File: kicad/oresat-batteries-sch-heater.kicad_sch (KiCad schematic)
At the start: 20 parts, among them Q20 PMV45EN, Q21 PMV45EN, Q38 PMV45EN, Q39 PMV45EN, Q42 MOSFET-PCH-SOT23-6, Q43 MOSFET-PCH-SOT23-6

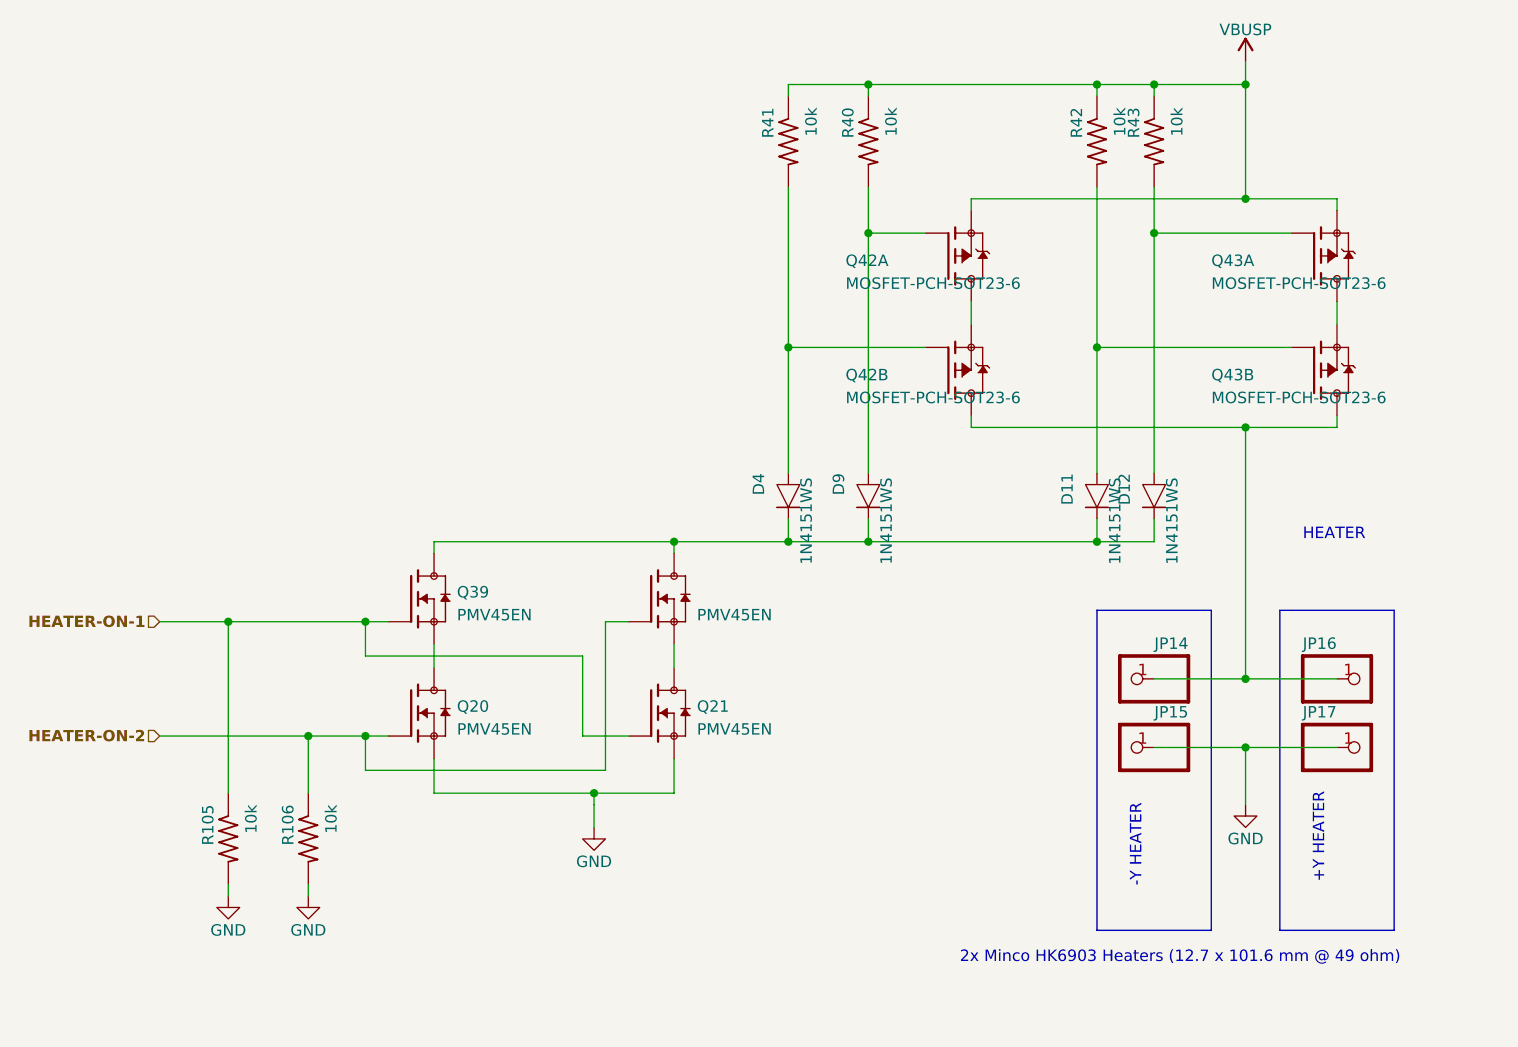
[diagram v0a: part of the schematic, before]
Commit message: Renovated Schematic
Updated schematic symbols and made more uniform with changed resistor, capacitor, and FET symbols. Changed 0603 cap foot print to 0603 small in Oresat passives. Added 2 new resistors and 2 new caps in the power page. Removed old debug connector in favor of the new one. The changes made should make very little updates when pushing the changes to the PCB.
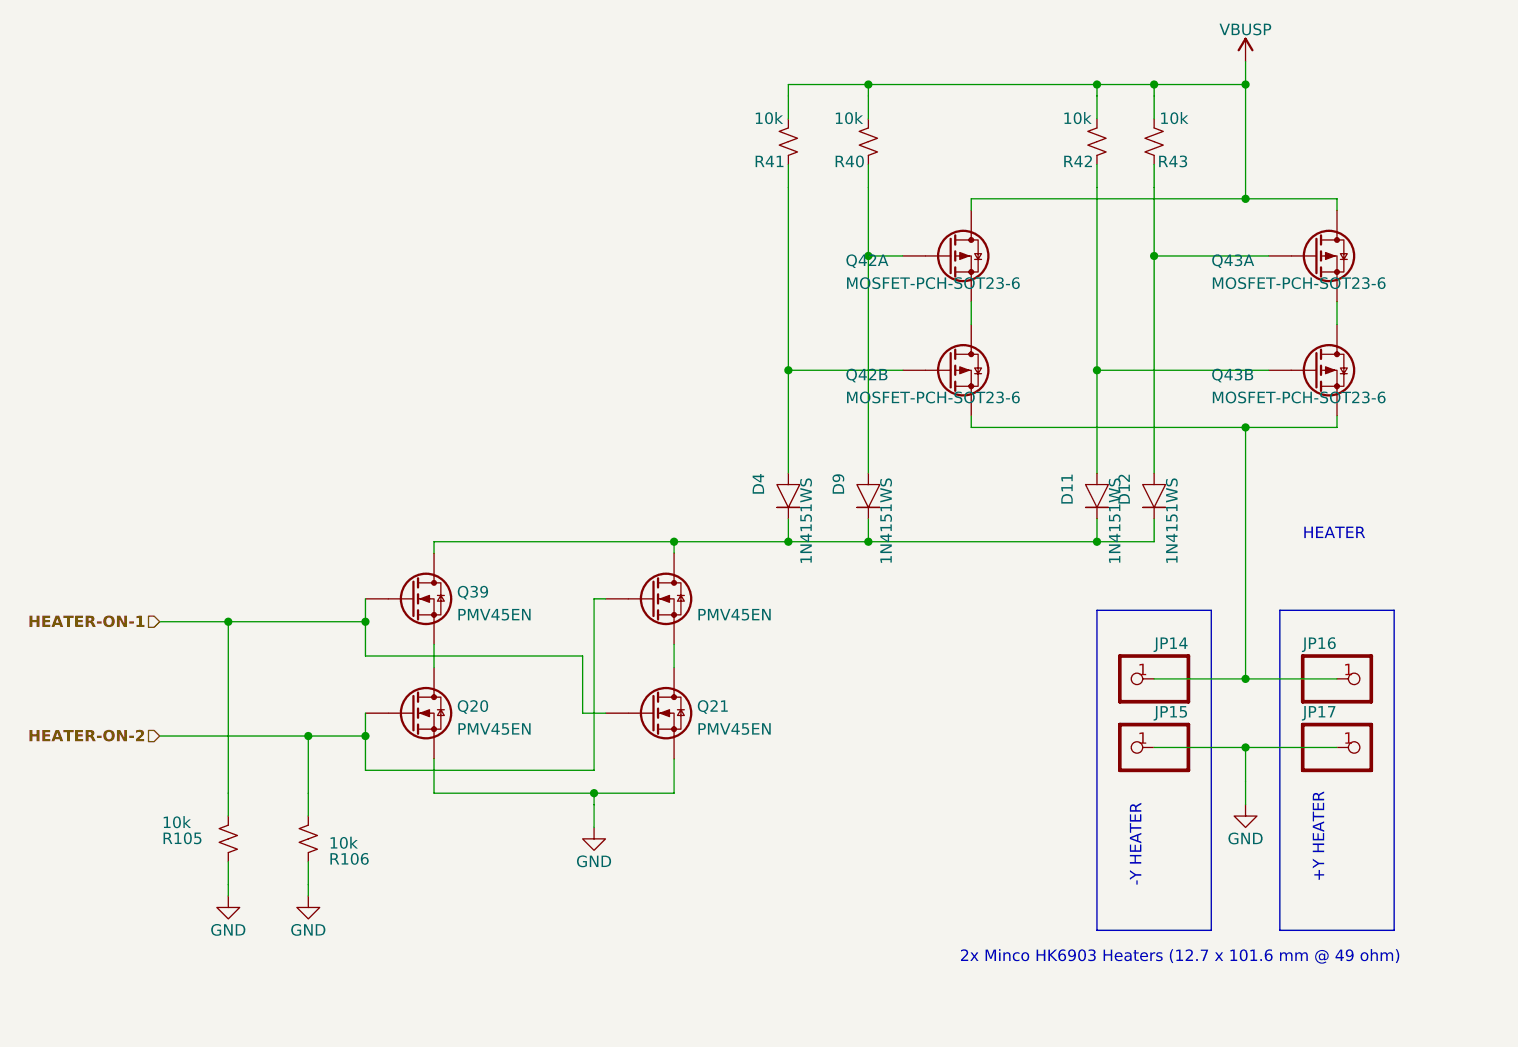
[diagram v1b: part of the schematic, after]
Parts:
- Q20, Q21, Q38, Q39: symbol oresat-batteries-eagle-import:N-MOSFET-SOT-23-3 -> Transistor_FET:Q_NMOS_GSD
- Q42, Q43: symbol oresat-batteries-eagle-import:Q-MOSFET-PCH-dual-SOT23-6_MOSFET-PCH-SOT23-6 -> Transistor_FET:Q_Dual_PMOS_G1S2G2D2S1D1
- R105, R106, R40, R41, R42, R43: symbol oresat-batteries-eagle-import:R-US_0603-C-NOSILK -> Device:R_Small_US
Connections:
- net GND: now also R105.1, R106.1; no longer R105.2, R106.2
- net HEATER-ON-1: now also R105.2; no longer R105.1
- net HEATER-ON-2: now also R106.2; no longer R106.1
- net VBUSP: now also Q42.6 (D), Q43.6 (D), R40.2, R41.2, R42.2, R43.2; no longer Q42.5 (S), Q43.5 (S), R40.1, R41.1, R42.1, R43.1
- net at D12.2, Q43.1 (G): now also R43.1; no longer R43.2
- net at Q42.2 (S): now also JP14.1, JP16.1, Q43.2 (S); no longer Q42.6 (D)
- net at D4.2, Q42.3 (G): now also R41.1; no longer R41.2
- net at D9.2, Q42.1 (G): now also R40.1; no longer R40.2
- net at D11.2, Q43.3 (G): now also R42.1; no longer R42.2
- new net: Q42.4 (D), Q42.5 (S)
- new net: Q43.4 (D), Q43.5 (S)

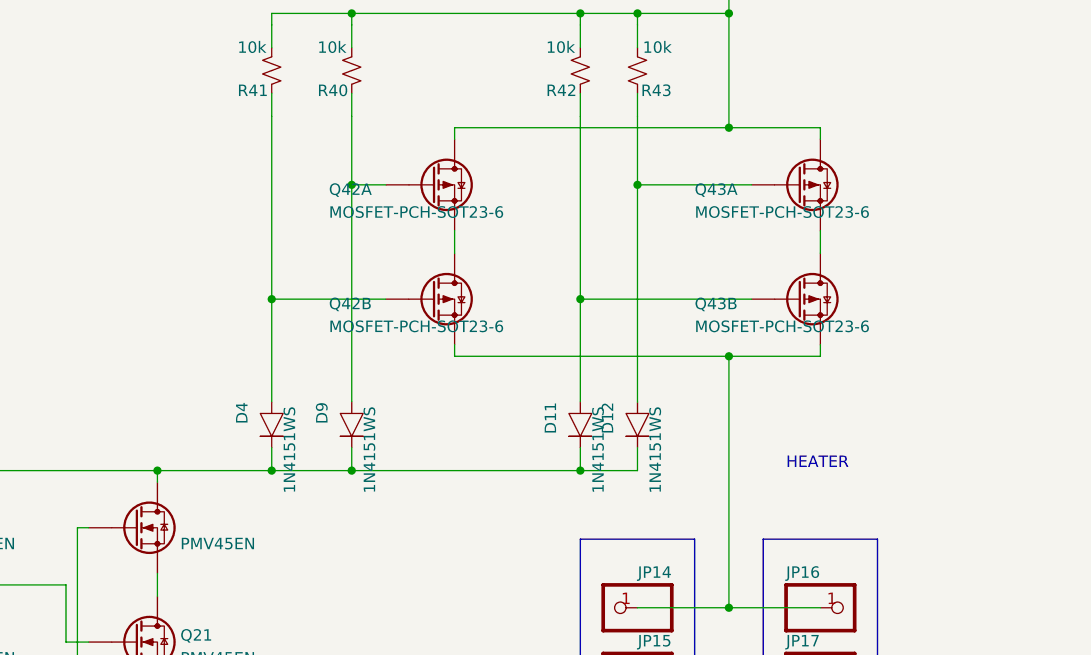
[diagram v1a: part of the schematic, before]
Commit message: Progress on v4
Figure out to bypass negative battery cutoff with 10k to make sure that nSHUTDOWN always works. Lots of moving around (it's tight), finally got pack 1 done. Working on the Pack 2.
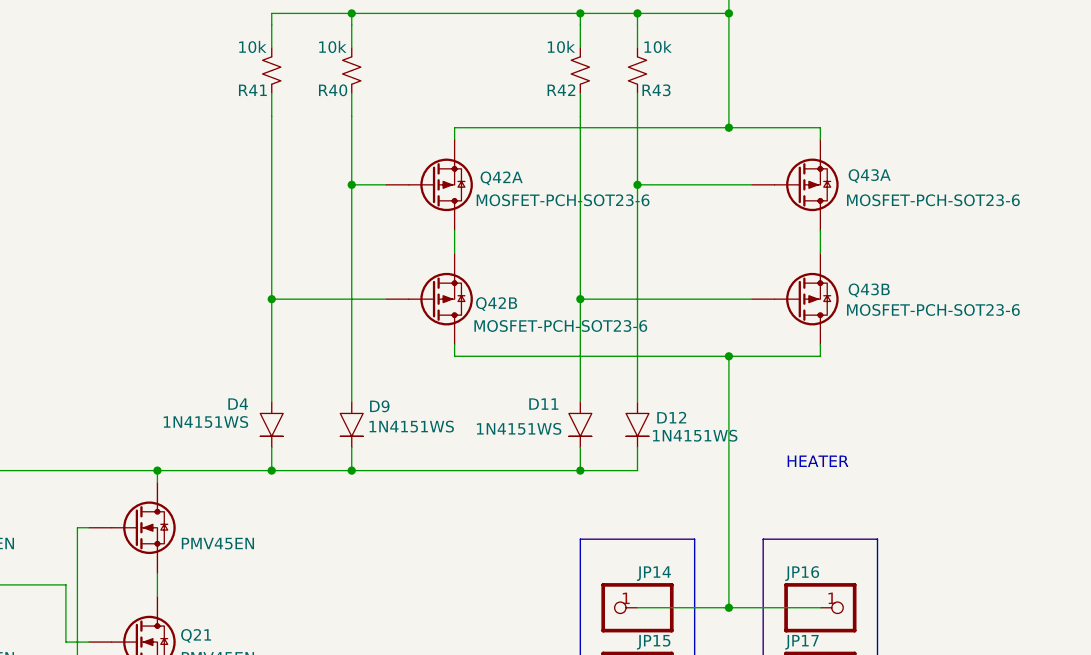
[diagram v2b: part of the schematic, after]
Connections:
- net VBUSP: now also Q42.5 (S), Q43.5 (S); no longer Q42.6 (D), Q43.6 (D)
- net at JP14.1, JP16.1: now also Q42.4 (D), Q43.4 (D); no longer Q42.2 (S), Q43.2 (S)
- new net: Q42.2 (S), Q42.6 (D)
- new net: Q43.2 (S), Q43.6 (D)
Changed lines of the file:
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@@
 		(dnp no)
 		(property "Reference" "D12"
-			(at 252.73 118.11 0)
+			(at 260.858 120.65 90)
 			(effects
 				(font
@@
 		)
 		(property "Value" "1N4151WS"
-			(at 256.54 128.27 0)
+			(at 256.794 121.158 90)
 			(effects
 				(font
@@
 		(lib_id "Transistor_FET:Q_Dual_PMOS_G1S2G2D2S1D1")
 		(at 232.41 106.68 0)
+		(mirror x)
 		(unit 2)
 		(exclude_from_sim no)
@@
 		(dnp no)
 		(property "Reference" "Q42"
-			(at 220.98 107.95 0)
+			(at 237.236 106.426 0)
 			(effects
 				(font
@@
 		)
 		(property "Value" "MOSFET-PCH-SOT23-6"
-			(at 220.98 110.49 0)
+			(at 236.982 108.966 0)
 			(effects
 				(font
@@
 		(dnp no)
 		(property "Reference" "D9"
-			(at 220.98 118.11 0)
+			(at 227.838 119.38 90)
 			(effects
 				(font
@@
 		)
 		(property "Value" "1N4151WS"
-			(at 224.79 128.27 0)
+			(at 225.298 120.142 90)
 			(effects
 				(font
@@
 		(lib_id "Transistor_FET:Q_Dual_PMOS_G1S2G2D2S1D1")
 		(at 273.05 106.68 0)
+		(mirror x)
 		(unit 2)
 		(exclude_from_sim no)
@@
 		(dnp no)
 		(property "Reference" "Q43"
-			(at 261.62 107.95 0)
+			(at 278.638 104.902 0)
 			(effects
 				(font
@@
 		)
 		(property "Value" "MOSFET-PCH-SOT23-6"
-			(at 261.62 110.49 0)
+			(at 278.384 107.188 0)
 			(effects
 				(font
@@
 		(dnp no)
 		(property "Reference" "D11"
-			(at 246.38 118.11 0)
+			(at 246.634 119.126 90)
 			(effects
 				(font
@@
 		)
 		(property "Value" "1N4151WS"
-			(at 250.19 128.27 0)
+			(at 237.236 120.396 90)
 			(effects
 				(font
@@
 		(lib_id "Transistor_FET:Q_Dual_PMOS_G1S2G2D2S1D1")
 		(at 273.05 93.98 0)
+		(mirror x)
 		(unit 1)
 		(exclude_from_sim no)
@@
 		(dnp no)
 		(property "Reference" "Q43"
-			(at 261.62 95.25 0)
+			(at 278.638 92.202 0)
 			(effects
 				(font
@@
 		)
 		(property "Value" "MOSFET-PCH-SOT23-6"
-			(at 261.62 97.79 0)
+			(at 278.384 94.996 0)
 			(effects
 				(font
@@
 		(lib_id "Transistor_FET:Q_Dual_PMOS_G1S2G2D2S1D1")
 		(at 232.41 93.98 0)
+		(mirror x)
 		(unit 1)
 		(exclude_from_sim no)
@@
 		(dnp no)
 		(property "Reference" "Q42"
-			(at 220.98 95.25 0)
+			(at 237.744 92.456 0)
 			(effects
 				(font
@@
 		)
 		(property "Value" "MOSFET-PCH-SOT23-6"
-			(at 220.98 97.79 0)
+			(at 237.236 94.996 0)
 			(effects
 				(font
@@
 		(dnp no)
 		(property "Reference" "D4"
-			(at 212.09 118.11 0)
+			(at 212.09 119.126 90)
 			(effects
 				(font
@@
 		)
 		(property "Value" "1N4151WS"
-			(at 215.9 128.27 0)
-			(effects
-				(font
+			(at 202.438 119.634 90)
+			(effects
+				(font
